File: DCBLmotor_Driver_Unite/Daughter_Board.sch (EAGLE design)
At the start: 64 parts, among them CN1 DF11-16DP-2DSA, CN2 26-01-3115, CN3 39-28-1023, IC1 ACS780KLRTR-150B-T, IC2 IR2010SPBF, IC3 IR2010SPBF, IC4 IR2010SPBF, IC5 ACS780KLRTR-150B-T, IC6 ACS780KLRTR-150B-T

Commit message: Version1 per finshed
Per complete Version1
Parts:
- added CN4: (no value), jst-xh:B2B-XH-A
- added PMC4: 50ST104MA13216, Rubycon:50ST104MA13216
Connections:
- new net N$31: DC-DC1.SS, PMC4.1
- net +20V: now also CN4.1
- net GND: now also CN4.2, PMC4.2
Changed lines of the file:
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@@
 <part name="R8" library="ROHM" deviceset="MCR03" device=""/>
 <part name="D1" library="DIODE" deviceset="1N5711W-7-F" device=""/>
+<part name="PMC4" library="Rubycon" deviceset="50ST104MA13216" device=""/>
+<part name="CN4" library="jst-xh" deviceset="B2B-XH-A" device=""/>
 </parts>
 <sheets>
@@
 <instance part="R8" gate="G$1" x="-40.64" y="-170.18"/>
 <instance part="D1" gate="G$1" x="-58.42" y="-170.18" rot="R90"/>
+<instance part="PMC4" gate="G$1" x="-91.44" y="-175.26"/>
+<instance part="CN4" gate="G$1" x="-22.86" y="-195.58" rot="R270"/>
 </instances>
 <busses>
@@
 <wire x1="-119.38" y1="-182.88" x2="-116.84" y2="-182.88" width="0.1524" layer="91"/>
 <wire x1="-116.84" y1="-182.88" x2="-109.22" y2="-182.88" width="0.1524" layer="91"/>
-<wire x1="-109.22" y1="-182.88" x2="-81.28" y2="-182.88" width="0.1524" layer="91"/>
+<wire x1="-109.22" y1="-182.88" x2="-91.44" y2="-182.88" width="0.1524" layer="91"/>
+<wire x1="-91.44" y1="-182.88" x2="-81.28" y2="-182.88" width="0.1524" layer="91"/>
 <wire x1="-81.28" y1="-182.88" x2="-81.28" y2="-170.18" width="0.1524" layer="91"/>
 <pinref part="C16" gate="G$1" pin="2"/>
@@
 <wire x1="-55.88" y1="-177.8" x2="-55.88" y2="-182.88" width="0.1524" layer="91"/>
 <junction x="-55.88" y="-182.88"/>
-<wire x1="-30.48" y1="-182.88" x2="-17.78" y2="-182.88" width="0.1524" layer="91"/>
+<wire x1="-30.48" y1="-182.88" x2="-25.4" y2="-182.88" width="0.1524" layer="91"/>
 <junction x="-30.48" y="-182.88"/>
 <pinref part="D1" gate="G$1" pin="A"/>
 <label x="-20.32" y="-182.88" size="1.778" layer="95"/>
+<pinref part="PMC4" gate="G$1" pin="2"/>
+<wire x1="-25.4" y1="-182.88" x2="-17.78" y2="-182.88" width="0.1524" layer="91"/>
+<wire x1="-91.44" y1="-180.34" x2="-91.44" y2="-182.88" width="0.1524" layer="91"/>
+<junction x="-91.44" y="-182.88"/>
+<pinref part="CN4" gate="G$1" pin="2"/>
+<wire x1="-25.4" y1="-195.58" x2="-25.4" y2="-182.88" width="0.1524" layer="91"/>
+<junction x="-25.4" y="-182.88"/>
 </segment>
 <segment>
@@
 <label x="-20.32" y="-152.4" size="1.778" layer="95"/>
 <pinref part="R8" gate="G$1" pin="1"/>
-<wire x1="-30.48" y1="-152.4" x2="-20.32" y2="-152.4" width="0.1524" layer="91"/>
+<wire x1="-30.48" y1="-152.4" x2="-22.86" y2="-152.4" width="0.1524" layer="91"/>
+<wire x1="-22.86" y1="-152.4" x2="-20.32" y2="-152.4" width="0.1524" layer="91"/>
 <wire x1="-35.56" y1="-170.18" x2="-35.56" y2="-152.4" width="0.1524" layer="91"/>
 <junction x="-35.56" y="-152.4"/>
@@
 <wire x1="-30.48" y1="-157.48" x2="-30.48" y2="-152.4" width="0.1524" layer="91"/>
 <junction x="-30.48" y="-152.4"/>
+<pinref part="CN4" gate="G$1" pin="1"/>
+<wire x1="-22.86" y1="-195.58" x2="-22.86" y2="-152.4" width="0.1524" layer="91"/>
+<junction x="-22.86" y="-152.4"/>
 </segment>
 </net>
@@
 </segment>
 </net>
+<net name="N$31" class="0">
+<segment>
+<pinref part="DC-DC1" gate="G$1" pin="SS"/>
+<pinref part="PMC4" gate="G$1" pin="1"/>
+<wire x1="-91.44" y1="-170.18" x2="-91.44" y2="-172.72" width="0.1524" layer="91"/>
+</segment>
+</net>

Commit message: Assigned Parts No.
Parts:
- added R10, R11, R12, R13, R14, R9: ESR03EZPJ753, ROHM:ESR03EZPJ753
- DC1, DC2, DC3, DC4, DC5, DC6: value YFF21PC -> YFF21PC1E104MT000N; device TDK:YFF21PC -> TDK:YFF21PC1E104MT000N
- R1, R2, R3, R4, R5, R6: value MCR03 -> ESR03EZPJ102; device ROHM:MCR03 -> ROHM:ESR03EZPJ102
- R7: value MCR03 -> RN55C8000BB14; device ROHM:MCR03 -> VISHAY:RN55C8000BB14
- R8: value MCR03 -> RN55C1912BB14; device ROHM:MCR03 -> VISHAY:RN55C1912BB14
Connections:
- removed net N$2: C11.1, IC4.COM
- removed net N$22: C7.2, FD7.A, IC2.VCC
- removed net N$24: C9.2, FD8.A, IC3.VCC
- removed net N$26: C11.2, FD9.A, IC4.VCC
- removed net N$4: C9.1, IC3.COM
- removed net N$6: C7.1, IC2.COM
- net +20V: now also C11.2, C7.2, C9.2, FD7.A, FD8.A, FD9.A, IC2.VCC, IC3.VCC, IC4.VCC
- net GND: now also C11.1, C7.1, C9.1, IC2.COM, IC3.COM, IC4.COM
- net N$14: now also R13.1
- net N$15: now also R12.2
- net N$18: now also R12.1
- net N$19: now also R11.1
- net N$20: now also R10.1
- net N$21: now also R9.1
- net N$3: now also R14.2
- net N$5: now also R13.2
- net N$9: now also R14.1
- net VS1: now also R9.2
- net VS2: now also R10.2
- net VS3: now also R11.2

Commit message: Change Driver borard
Change FETs and Gatedriver
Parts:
- removed C10, C11, C12, C7, C8, C9: C2012JB0J476M125AC, TDK:C2012JB0J476M125AC
- removed C13, C14, C15: CGA1A2C0G1E180J030BA, TDK:CGA1A2C0G1E180J030BA
- removed C16: MAL202117152E3, VISHAY:MAL202117152E3
- removed C17: T495D475K050ATE275, KEMET:T495D475K050ATE275
- removed C18: T494X107M025AT, KEMET:T494X107M025AT
- removed C2, C3: KTD500B227M99A0B00, United_Chemi-con:KTD500B227M99A0B00
- removed CN4: (no value), jst-xh:B2B-XH-A
- removed D1: 1N5711W-7-F, DIODE:1N5711W-7-F
- removed DC-DC1: SI-8008HD-TL, SANKEN:SI-8008HD-TL
- removed DC1, DC2, DC3, DC4, DC5, DC6: YFF21PC1E104MT000N, TDK:YFF21PC1E104MT000N
- removed FD7, FD8, FD9: 1N4448WQ-7-F, DIODE:1N4448WQ-7-F
- removed IC5, IC6: ACS780KLRTR-150B-T, ACS780:ACS780KLRTR-150B-T
- removed L1: SRR1260-100M, Bourns:SRR1260-100M
- removed PMC4: 50ST104MA13216, Rubycon:50ST104MA13216
- removed R7: RN55C8000BB14, VISHAY:RN55C8000BB14
- removed R8: RN55C1912BB14, VISHAY:RN55C1912BB14
- C1: value KTD500B227M99A0B00 -> T494X107M025AT; device United_Chemi-con:KTD500B227M99A0B00 -> KEMET:T494X107M025AT
- FET1, FET2, FET3, FET4, FET5, FET6: value IRF7739L1TRPBF -> IRF7480MTRPBF; device Infinion:IRF7739L1TRPBF -> Infinion:IRF7480MTRPBF
- IC1: value ACS780KLRTR-150B-T -> IR25750LPBF; device ACS780:ACS780KLRTR-150B-T -> Infinion:IR25750LPBF
- IC2, IC3: value IR2010SPBF -> IR25750LPBF; device IR2010SPBF:IR2010SPBF -> Infinion:IR25750LPBF
- IC4: value IR2010SPBF -> DRV8320SRTVT; device IR2010SPBF:IR2010SPBF -> DRV8320SRTVT:DRV8320SRTVT
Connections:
- removed net +20V: C11.2, C18.+, C7.2, C9.2, CN4.1, DC1.P$2, DC2.P$2, DC3.P$2, FD7.A, FD8.A, FD9.A, IC2.VCC, IC3.VCC, IC4.VCC, L1.2, R8.1
- removed net N$10: DC5.P$1, IC5.VCC
- removed net N$14: FET4.G, R13.1, R5.1
- removed net N$15: FD6.A, FET6.S, IC6.IP+, R12.2
- removed net N$16: DC6.P$1, IC6.VCC
- removed net N$17: DC-DC1.ADJ, R7.2, R8.2
- removed net N$23: C8.1, FD7.C, IC2.VB
- removed net N$25: C10.1, FD8.C, IC3.VB
- removed net N$27: C12.1, FD9.C, IC4.VB
- removed net N$28: DC2.P$1, IC3.VDD
- removed net N$29: DC3.P$1, IC4.VDD
- removed net N$3: FD2.A, FET2.S, IC1.IP+, R14.2
- removed net N$30: DC1.P$1, IC2.VDD
- removed net N$31: DC-DC1.SS, PMC4.1
- removed net N$5: FD4.A, FET4.S, IC5.IP+, R13.2
- removed net N$7: DC4.P$1, IC1.VCC
- removed net N$8: D1.C, DC-DC1.SW, L1.1
- removed net N$9: FET2.G, R14.1, R6.1
- new net N$2: FET4.G, IC2.GATE, R13.2, R5.1
- new net N$4: FET2.G, R6.1
- new net N$6: IC1.GATE, R14.2
- net +5V: no longer DC4.P$2, DC5.P$2, DC6.P$2
- net CU1: no longer C13.1, IC1.VOUT
- net CU2: no longer C14.1, IC5.VOUT
- net CU3: no longer C15.1, IC6.VOUT
- net GND: now also FD2.A, FD4.A, FD6.A, FET2.S, FET4.S, FET6.S, R12.1, R13.1; no longer C11.1, C16.2, C17.2, C18.2, C2.2, C3.2, C7.1, C9.1, CN4.2, D1.A, DC-DC1.GND, DC1.GND, DC2.GND, DC3.GND, IC1.IP-, IC2.VSS, IC3.VSS, IC4.COM, IC4.VSS, IC5.IP-, IC6.IP-, PMC4.2, R7.1
- net GND_LG: no longer C13.2, C14.2, C15.2, DC4.GND, DC5.GND, DC6.GND, IC1.GND, IC5.GND, IC6.GND
- net HIN1: no longer IC2.HIN
- net HIN2: no longer IC3.HIN
- net HIN3: no longer IC4.HIN
- net HO1: no longer IC2.HO
- net HO2: no longer IC3.HO
- net HO3: no longer IC4.HO
- net LIN1: no longer IC2.LIN
- net LIN2: no longer IC3.LIN
- net LIN3: no longer IC4.LIN
- net LO1: no longer IC2.LO
- net LO2: no longer IC3.LO
- net LO3: no longer IC4.LO
- net N$18: now also IC3.GATE, R12.2; no longer R12.1
- net SD: no longer IC2.SD, IC3.SD, IC4.SD
- net VCC: now also C1.+; no longer C1.1, C16.+, C17.+, C2.1, C3.1, DC-DC1.IN
- net VS1: now also IC1.VS; no longer C8.2, IC2.VS
- net VS2: now also IC2.VS; no longer C10.2, IC3.VS
- net VS3: now also IC3.VS; no longer C12.2, IC4.VS
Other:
- moved on the sheet: FD1, FD2, FD3, FD4, FD5, FD6, R12, R13, R14, R4, R5, R6

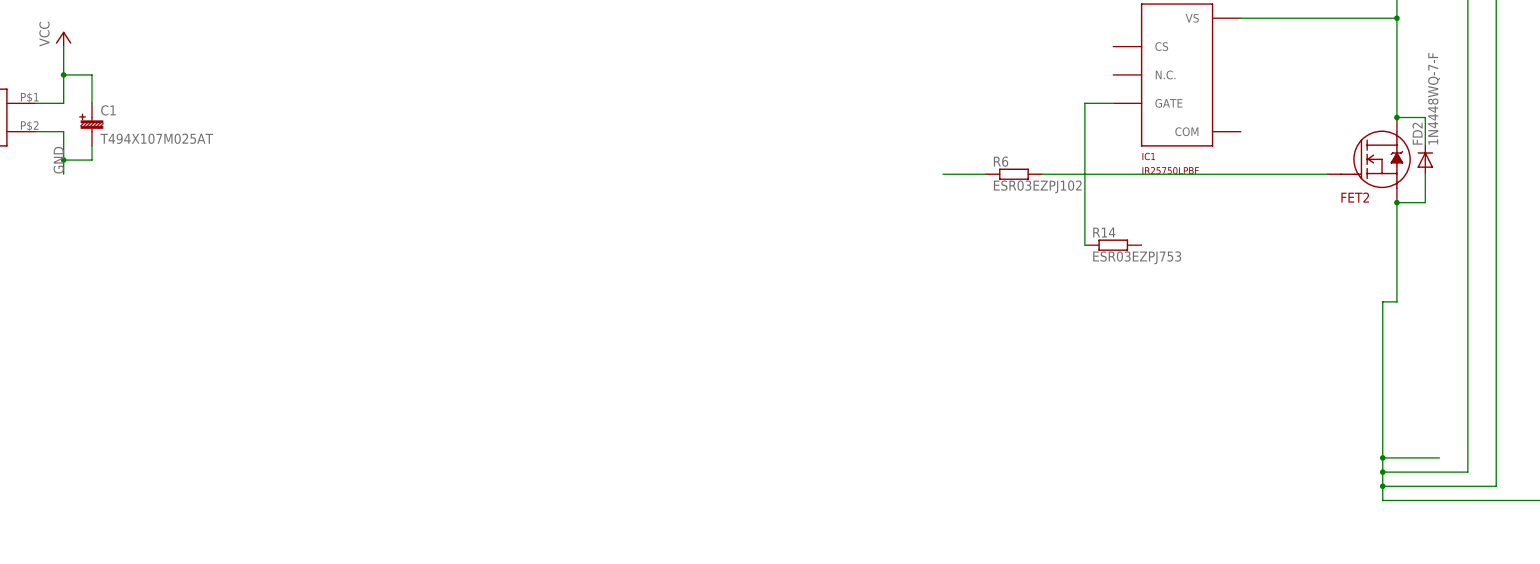
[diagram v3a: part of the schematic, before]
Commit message: Build around FET
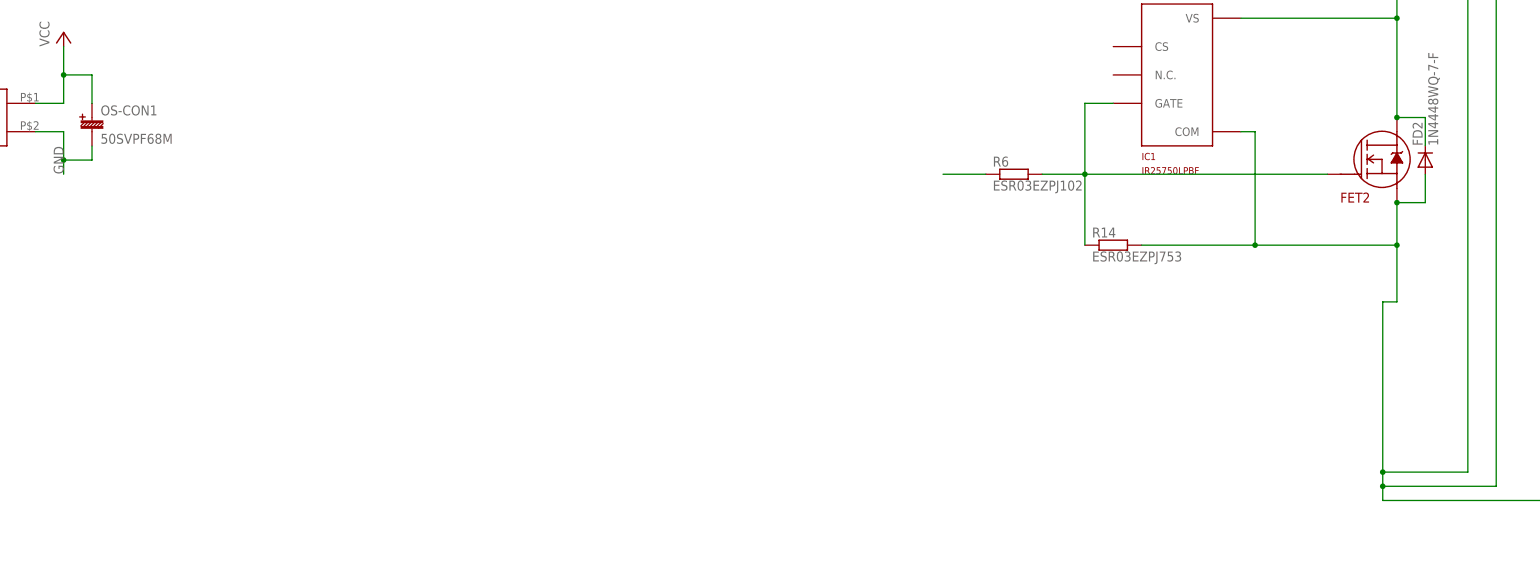
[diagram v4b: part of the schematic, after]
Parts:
- removed C1: T494X107M025AT, KEMET:T494X107M025AT
- added OS-CON1: 50SVPF68M, OS-CON:50SVPF68M
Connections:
- removed net N$6: IC1.GATE, R14.2
- net GND: now also IC1.COM, OS-CON1.2, R14.1; no longer C1.2
- net N$4: now also IC1.GATE, R14.2
- net VCC: now also OS-CON1.+; no longer C1.+
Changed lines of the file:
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@@
 <part name="IC3" library="Infinion" deviceset="IR25750LPBF" device=""/>
 <part name="IC4" library="DRV8320SRTVT" deviceset="DRV8320SRTVT" device=""/>
-<part name="C1" library="KEMET" deviceset="T494X107M025AT" device=""/>
+<part name="OS-CON1" library="OS-CON" deviceset="50SVPF68M" device=""/>
 </parts>
 <sheets>
@@
 <instance part="IC3" gate="G$1" x="50.8" y="-33.02"/>
 <instance part="IC4" gate="G$1" x="-66.04" y="-73.66"/>
-<instance part="C1" gate="G$1" x="-142.24" y="-139.7"/>
+<instance part="OS-CON1" gate="G$1" x="-142.24" y="-139.7"/>
 </instances>
 <busses>
@@
 <wire x1="104.14" y1="-203.2" x2="88.9" y2="-203.2" width="0.1524" layer="91"/>
 <junction x="88.9" y="-203.2"/>
-<wire x1="88.9" y1="-203.2" x2="88.9" y2="-200.66" width="0.1524" layer="91"/>
 <wire x1="162.56" y1="-203.2" x2="177.8" y2="-203.2" width="0.1524" layer="91"/>
 <junction x="162.56" y="-203.2"/>
@@
 <wire x1="259.08" y1="-205.74" x2="259.08" y2="-7.62" width="0.1524" layer="91"/>
 <junction x="236.22" y="-205.74"/>
-<wire x1="88.9" y1="-200.66" x2="99.06" y2="-200.66" width="0.1524" layer="91"/>
-<junction x="88.9" y="-200.66"/>
 <pinref part="FD2" gate="G$1" pin="A"/>
-<wire x1="88.9" y1="-200.66" x2="88.9" y2="-172.72" width="0.1524" layer="91"/>
+<wire x1="88.9" y1="-203.2" x2="88.9" y2="-172.72" width="0.1524" layer="91"/>
 <wire x1="91.44" y1="-172.72" x2="88.9" y2="-172.72" width="0.1524" layer="91"/>
 <pinref part="FET2" gate="G$1" pin="S"/>
-<wire x1="91.44" y1="-154.94" x2="91.44" y2="-172.72" width="0.1524" layer="91"/>
+<wire x1="91.44" y1="-154.94" x2="91.44" y2="-162.56" width="0.1524" layer="91"/>
 <junction x="91.44" y="-154.94"/>
+<wire x1="91.44" y1="-162.56" x2="91.44" y2="-172.72" width="0.1524" layer="91"/>
 <wire x1="91.44" y1="-154.94" x2="96.52" y2="-154.94" width="0.1524" layer="91"/>
 <wire x1="96.52" y1="-154.94" x2="96.52" y2="-149.86" width="0.1524" layer="91"/>
@@
 <wire x1="66.04" y1="-43.18" x2="66.04" y2="-66.04" width="0.1524" layer="91"/>
 <junction x="66.04" y="-66.04"/>
+<pinref part="R14" gate="G$1" pin="1"/>
+<wire x1="45.72" y1="-162.56" x2="66.04" y2="-162.56" width="0.1524" layer="91"/>
+<junction x="91.44" y="-162.56"/>
+<pinref part="IC1" gate="G$1" pin="COM"/>
+<wire x1="66.04" y1="-162.56" x2="91.44" y2="-162.56" width="0.1524" layer="91"/>
+<wire x1="63.5" y1="-142.24" x2="66.04" y2="-142.24" width="0.1524" layer="91"/>
+<wire x1="66.04" y1="-142.24" x2="66.04" y2="-162.56" width="0.1524" layer="91"/>
+<junction x="66.04" y="-162.56"/>
 </segment>
 <segment>
@@
 <wire x1="-147.32" y1="-142.24" x2="-147.32" y2="-147.32" width="0.1524" layer="91"/>
 <label x="-147.32" y="-149.86" size="1.778" layer="95" rot="R90"/>
-<pinref part="C1" gate="G$1" pin="2"/>
 <wire x1="-147.32" y1="-147.32" x2="-147.32" y2="-149.86" width="0.1524" layer="91"/>
 <wire x1="-142.24" y1="-144.78" x2="-142.24" y2="-147.32" width="0.1524" layer="91"/>
 <wire x1="-142.24" y1="-147.32" x2="-147.32" y2="-147.32" width="0.1524" layer="91"/>
 <junction x="-147.32" y="-147.32"/>
+<pinref part="OS-CON1" gate="G$1" pin="2"/>
 </segment>
 </net>
@@
 <wire x1="-152.4" y1="-137.16" x2="-147.32" y2="-137.16" width="0.1524" layer="91"/>
 <wire x1="-147.32" y1="-137.16" x2="-147.32" y2="-132.08" width="0.1524" layer="91"/>
-<pinref part="C1" gate="G$1" pin="+"/>
 <wire x1="-147.32" y1="-132.08" x2="-147.32" y2="-127" width="0.1524" layer="91"/>
 <wire x1="-142.24" y1="-137.16" x2="-142.24" y2="-132.08" width="0.1524" layer="91"/>
 <wire x1="-142.24" y1="-132.08" x2="-147.32" y2="-132.08" width="0.1524" layer="91"/>
 <junction x="-147.32" y="-132.08"/>
+<pinref part="OS-CON1" gate="G$1" pin="+"/>
 </segment>
 </net>
@@
 <pinref part="R6" gate="G$1" pin="1"/>
 <pinref part="FET2" gate="G$1" pin="G"/>
-<wire x1="27.94" y1="-149.86" x2="78.994" y2="-149.86" width="0.1524" layer="91"/>
-</segment>
-</net>
-<net name="N$6" class="0">
-<segment>
+<wire x1="27.94" y1="-149.86" x2="35.56" y2="-149.86" width="0.1524" layer="91"/>
 <pinref part="IC1" gate="G$1" pin="GATE"/>
 <pinref part="R14" gate="G$1" pin="2"/>
+<wire x1="35.56" y1="-149.86" x2="78.994" y2="-149.86" width="0.1524" layer="91"/>
 <wire x1="40.64" y1="-137.16" x2="35.56" y2="-137.16" width="0.1524" layer="91"/>
-<wire x1="35.56" y1="-137.16" x2="35.56" y2="-162.56" width="0.1524" layer="91"/>
-</segment>
-</net>
+<wire x1="35.56" y1="-137.16" x2="35.56" y2="-149.86" width="0.1524" layer="91"/>
+<junction x="35.56" y="-149.86"/>
+<wire x1="35.56" y1="-149.86" x2="35.56" y2="-162.56" width="0.1524" layer="91"/>
+</segment>
+</net>

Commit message: Just before Delete MCU from daughter
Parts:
- removed CN1: DF11-16DP-2DSA, Hirose:DF11-16DP-2DSA
- removed CN3: 39-28-1023, Molex:39-28-1023
- removed R10, R11, R12, R13, R14, R9: ESR03EZPJ753, ROHM:ESR03EZPJ753
- removed RA1, RA2: EXB-38V103JV, Pana_Chip_RA:EXB-38V103JV
- added C1, C2: CKG32KX7R1H105M335AJ, TDK:CKG32KX7R1H105M335AJ
- added C10, C11: GRM0225C1E120JA03L, murata:GRM0225C1E120JA03L
- added C3: CGA2B3X7R1H473K050BB, TDK:CGA2B3X7R1H473K050BB
- added C7: 337CKS063M, Cornell Dubilier:337CKS063M
- added C8, C9: GRM035R60J475ME15D, murata:GRM035R60J475ME15D
- added CN4: DF63-3P-3.96DSA, Hirose:DF63-3P-3.96DSA
- added DC1, DC2, DC3, DC4: YFF15PC1C104MT000N, TDK:YFF15PC1C104MT000N
- added IC6: LTM8050IY#PBF-ND, LTM8050IY#PBF-ND:LTM8050IY#PBF-ND
- added IC7: TMPM373FWDUG, TMPM373FWDUG:TMPM373FWDUG
- added XTAL1: ABM8AIG-10.000MHZ-12-2Z-T3, Abracon:ABM8AIG-10.000MHZ-12-2Z-T3
- CN2: value 26-01-3115 -> DF63-2P-3.96DSA; device Molex:26-01-3115 -> Hirose:DF63-2P-3.96DSA
- OS-CON1: value 50SVPF68M -> 63SXE33M; device OS-CON:50SVPF68M -> OS-CON:63SXE33M
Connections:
- removed net +5V: CN1.16
- removed net GND_LG: CN1.12, RA1-1.2, RA1-2.2, RA1-3.2, RA1-4.2, RA2-1.2, RA2-2.2, RA2-3.2, RA2-4.2
- new net +3.3V: C2.2, DC1.P$1, DC2.P$2, DC4.P$2, IC4.DVDD, IC6.VOUT(1), IC6.VOUT(10), IC6.VOUT(11), IC6.VOUT(12), IC6.VOUT(13), IC6.VOUT(14), IC6.VOUT(15), IC6.VOUT(16), IC6.VOUT(2), IC6.VOUT(3), IC6.VOUT(4), IC6.VOUT(5), IC6.VOUT(6), IC6.VOUT(7), IC6.VOUT(8), IC6.VOUT(9)
- new net AGND: C2.1, IC4.AGND, IC4.PGND
- new net N$10: DC1.P$2, IC7.DVDD5(1)
- new net N$14: C9.1, IC7.VOUT3
- new net N$3: C11.1, IC7.PM0/X1, XTAL1.P$2
- new net N$5: C1.2, IC4.VCP
- new net N$6: DC2.P$1, IC7.RVDD5
- new net N$7: C3.2, IC4.CPH
- new net N$8: C3.1, IC4.CPL
- new net N$9: DC4.P$1, IC7.DVDD5(2)
- net CU1: now also IC1.CS, IC7.PJ7/AINB10/INTD; no longer CN1.15
- net CU2: now also IC2.CS, IC7.PK0/AINB11/INTD; no longer CN1.14
- net CU3: now also IC3.CS, IC7.PK1/AINB12/INTF; no longer CN1.13
- net GND: now also C10.2, C11.2, C7.2, C8.2, C9.2, CN2.1, DC1.GND, DC2.GND, DC4.GND, IC4.SLA, IC4.SLB, IC4.SLC, IC4.THERMAL_PAD, IC6.GND(1), IC6.GND(10), IC6.GND(11), IC6.GND(12), IC6.GND(13), IC6.GND(14), IC6.GND(15), IC6.GND(16), IC6.GND(17), IC6.GND(18), IC6.GND(19), IC6.GND(2), IC6.GND(20), IC6.GND(21), IC6.GND(22), IC6.GND(23), IC6.GND(24), IC6.GND(25), IC6.GND(26), IC6.GND(27), IC6.GND(28), IC6.GND(29), IC6.GND(3), IC6.GND(30), IC6.GND(31), IC6.GND(32), IC6.GND(33), IC6.GND(34), IC6.GND(35), IC6.GND(36), IC6.GND(37), IC6.GND(4), IC6.GND(5), IC6.GND(6), IC6.GND(7), IC6.GND(8), IC6.GND(9), IC7.DVSS(1), IC7.DVSS(2); no longer CN3.P$2, R12.1, R13.1, R14.1
- net HIN1: now also IC4.INHA, IC7.PG0/UO1; no longer CN1.3, RA2-4.1
- net HIN2: now also IC4.INHB, IC7.PG2/VO1; no longer CN1.5, RA1-2.1
- net HIN3: now also IC4.INHC, IC7.PG4/WO1; no longer CN1.7, RA1-4.1
- net HO1: now also IC4.GHA
- net HO2: now also IC4.GHB
- net HO3: now also IC4.GHC
- net LIN1: now also IC4.INLA, IC7.PG1/XO1; no longer CN1.4, RA2-3.1
- net LIN2: now also IC4.INLB, IC7.PG3/YO1; no longer CN1.6, RA1-1.1
- net LIN3: now also IC4.INLC, IC7.PG5/ZO1; no longer CN1.8, RA1-3.1
- net LO1: now also IC4.GLA
- net LO2: now also IC4.GLB
- net LO3: now also IC4.GLC
- net N$1: now also C10.1, IC7.PM1/X2, XTAL1.P$1; no longer CN1.1, RA2-1.1
- net N$11: now also DC3.P$1, IC7.AVDD5B/VREFHB; no longer CN1.9
- net N$12: now also DC3.GND, IC7.AVSSB/VREFB; no longer CN1.10
- net N$13: now also C8.1, IC7.VOUT15; no longer CN1.11
- net N$18: no longer R12.2
- net N$19: no longer R11.1
- net N$2: no longer R13.2
- net N$20: no longer R10.1
- net N$21: no longer R9.1
- net N$4: no longer R14.2
- net SD: now also IC4.ENABLE; no longer CN1.2, RA2-2.1
- net VCC: now also C1.1, C7.+, CN2.2, IC4.VDRAIN, IC4.VM, IC6.PGOOD, IC6.VIN(1), IC6.VIN(2), IC6.VIN(3), IC6.VIN(4), IC6.VIN(5), IC6.VIN(6), IC6.VIN(7), IC6.VIN(8), IC6.VIN(9); no longer CN3.P$1
- net VS1: now also CN4.1, IC4.SHA; no longer CN2.P$2, R9.2
- net VS2: now also CN4.2, IC4.SHB; no longer CN2.P$3, R10.2
- net VS3: now also CN4.3, IC4.SHC; no longer CN2.P$1, R11.2
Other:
- moved on the sheet: C5, FD1, FD3, FD5, FD6, FET1, FET3, FET5, FET6, PMC2, R1
